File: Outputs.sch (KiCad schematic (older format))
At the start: 19 parts, among them P10 CONN_6, P11 CONN_8, P13 CONN_6, P8 CONN_8, P9 CONN_8

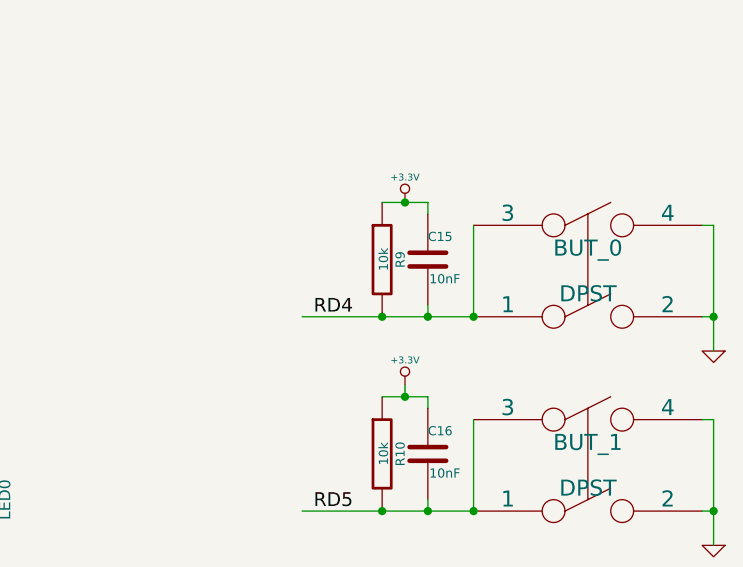
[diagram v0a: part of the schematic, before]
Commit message: This branch uses a MCP2200 rather than an FTDI chip
Signed-off-by: Kolijn Wolfaardt <kolijn.wolfaardt@gmail.com>
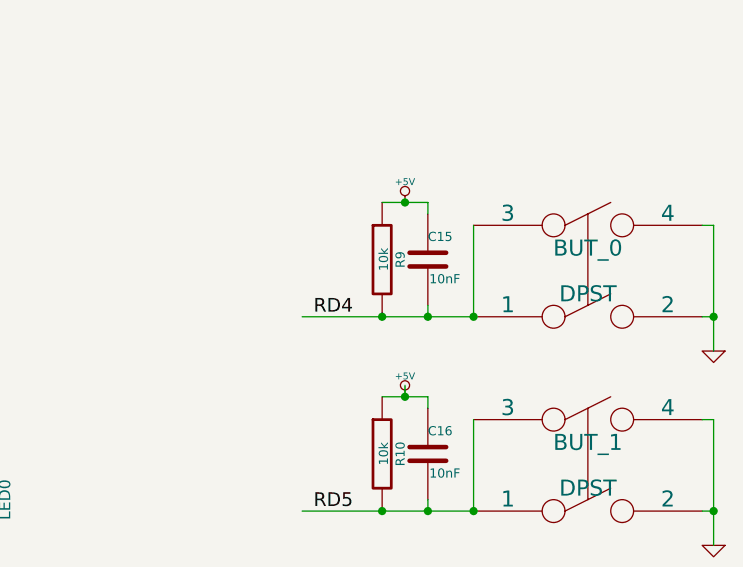
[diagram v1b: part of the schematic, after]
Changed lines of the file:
@@
 LIBS:FT230x
 LIBS:33vReg
+LIBS:mcp2200
 LIBS:Robotics Board-cache
 EELAYER 27 0
@@
 $EndComp
 $Comp
-L GND #PWR048
+L GND #PWR049
 U 1 1 52F7FC4E
 P 5500 5000
-F 0 "#PWR048" H 5500 5000 30  0001 C CNN
+F 0 "#PWR049" H 5500 5000 30  0001 C CNN
 F 1 "GND" H 5500 4930 30  0001 C CNN
 F 2 "" H 5500 5000 60  0000 C CNN
@@
 $EndComp
 $Comp
-L GND #PWR049
+L GND #PWR050
 U 1 1 52F7FE89
 P 9300 3400
-F 0 "#PWR049" H 9300 3400 30  0001 C CNN
+F 0 "#PWR050" H 9300 3400 30  0001 C CNN
 F 1 "GND" H 9300 3330 30  0001 C CNN
 F 2 "" H 9300 3400 60  0000 C CNN
@@
 $EndComp
 $Comp
-L GND #PWR050
+L GND #PWR051
 U 1 1 52F7FEB7
 P 9300 4250
-F 0 "#PWR050" H 9300 4250 30  0001 C CNN
+F 0 "#PWR051" H 9300 4250 30  0001 C CNN
 F 1 "GND" H 9300 4180 30  0001 C CNN
 F 2 "" H 9300 4250 60  0000 C CNN
@@
 $EndComp
 $Comp
-L GND #PWR051
+L GND #PWR052
 U 1 1 52F799A9
 P 7800 1450
-F 0 "#PWR051" H 7800 1450 30  0001 C CNN
+F 0 "#PWR052" H 7800 1450 30  0001 C CNN
 F 1 "GND" H 7800 1380 30  0001 C CNN
 F 2 "" H 7800 1450 60  0000 C CNN
@@
 V_5v
 $Comp
-L GND #PWR052
+L GND #PWR053
 U 1 1 52F79CA3
 P 5250 2150
-F 0 "#PWR052" H 5250 2150 30  0001 C CNN
+F 0 "#PWR053" H 5250 2150 30  0001 C CNN
 F 1 "GND" H 5250 2080 30  0001 C CNN
 F 2 "" H 5250 2150 60  0000 C CNN
@@
 V_batt
 $Comp
-L +BATT #PWR053
+L +BATT #PWR054
 U 1 1 52F79EEA
 P 5000 1300
-F 0 "#PWR053" H 5000 1250 20  0001 C CNN
+F 0 "#PWR054" H 5000 1250 20  0001 C CNN
 F 1 "+BATT" H 5000 1400 30  0000 C CNN
 F 2 "" H 5000 1300 60  0000 C CNN
@@
 Vdd
 $Comp
-L +5V #PWR054
+L +5V #PWR055
 U 1 1 52F7A111
 P 5100 1400
-F 0 "#PWR054" H 5100 1490 20  0001 C CNN
+F 0 "#PWR055" H 5100 1490 20  0001 C CNN
 F 1 "+5V" H 5100 1490 30  0000 C CNN
 F 2 "" H 5100 1400 60  0000 C CNN
@@
 $EndComp
 $Comp
-L +5V #PWR055
+L +5V #PWR056
 U 1 1 52F7A162
 P 7850 1150
-F 0 "#PWR055" H 7850 1240 20  0001 C CNN
+F 0 "#PWR056" H 7850 1240 20  0001 C CNN
 F 1 "+5V" H 7850 1240 30  0000 C CNN
 F 2 "" H 7850 1150 60  0000 C CNN
@@
 $EndComp
 $Comp
-L +BATT #PWR056
+L +BATT #PWR057
 U 1 1 52F7A168
 P 8000 1450
-F 0 "#PWR056" H 8000 1400 20  0001 C CNN
+F 0 "#PWR057" H 8000 1400 20  0001 C CNN
 F 1 "+BATT" H 8000 1550 30  0000 C CNN
 F 2 "" H 8000 1450 60  0000 C CNN
@@
 V3.3
 $Comp
-L +3.3V #PWR057
+L +3.3V #PWR058
 U 1 1 53538049
 P 5200 1500
-F 0 "#PWR057" H 5200 1460 30  0001 C CNN
+F 0 "#PWR058" H 5200 1460 30  0001 C CNN
 F 1 "+3.3V" H 5200 1610 30  0000 C CNN
 F 2 "" H 5200 1500 60  0000 C CNN
@@
 	5200 1700 5200 1500
 $Comp
-L +3.3V #PWR058
+L +3.3V #PWR059
 U 1 1 53538103
 P 7950 1050
-F 0 "#PWR058" H 7950 1010 30  0001 C CNN
+F 0 "#PWR059" H 7950 1010 30  0001 C CNN
 F 1 "+3.3V" H 7950 1160 30  0000 C CNN
 F 2 "" H 7950 1050 60  0000 C CNN
@@
 	7800 1250 8250 1250
 Connection ~ 8150 1250
-$Comp
-L +3.3V #PWR059
-U 1 1 535384DE
-P 7950 2750
-F 0 "#PWR059" H 7950 2710 30  0001 C CNN
-F 1 "+3.3V" H 7950 2860 30  0000 C CNN
-F 2 "" H 7950 2750 60  0000 C CNN
-F 3 "" H 7950 2750 60  0000 C CNN
-	1    7950 2750
-	1    0    0    -1
-$EndComp
 Wire Wire Line
 	7850 2750 8050 2750
@@
 $EndComp
 Wire Wire Line
-	8050 3600 7850 3600
-$Comp
-L +3.3V #PWR060
-U 1 1 535386B3
-P 7950 3550
-F 0 "#PWR060" H 7950 3510 30  0001 C CNN
-F 1 "+3.3V" H 7950 3660 30  0000 C CNN
-F 2 "" H 7950 3550 60  0000 C CNN
-F 3 "" H 7950 3550 60  0000 C CNN
-	1    7950 3550
-	1    0    0    -1
-$EndComp
+	7850 3600 8050 3600
 Wire Wire Line
 	7950 3550 7950 3600
 Connection ~ 7950 3600
+$Comp
+L +5V #PWR060
+U 1 1 53545316
+P 7950 2750
+F 0 "#PWR060" H 7950 2840 20  0001 C CNN
+F 1 "+5V" H 7950 2840 30  0000 C CNN
+F 2 "" H 7950 2750 60  0000 C CNN
+F 3 "" H 7950 2750 60  0000 C CNN
+	1    7950 2750
+	1    0    0    -1
+$EndComp
+$Comp
+L +5V #PWR061
+U 1 1 5354531C
+P 7950 3600
+F 0 "#PWR061" H 7950 3690 20  0001 C CNN
+F 1 "+5V" H 7950 3690 30  0000 C CNN
+F 2 "" H 7950 3600 60  0000 C CNN
+F 3 "" H 7950 3600 60  0000 C CNN
+	1    7950 3600
+	1    0    0    -1
+$EndComp
 $EndSCHEMATC
